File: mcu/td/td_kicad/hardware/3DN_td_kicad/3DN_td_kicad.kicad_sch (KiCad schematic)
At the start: 24 parts, among them J1 STLink, J2 ADC, J3 SPI, J4 I2C, J5 Conn_01x02, U1 STM32G031K8T6, U2 MIC5504-3.3YM5

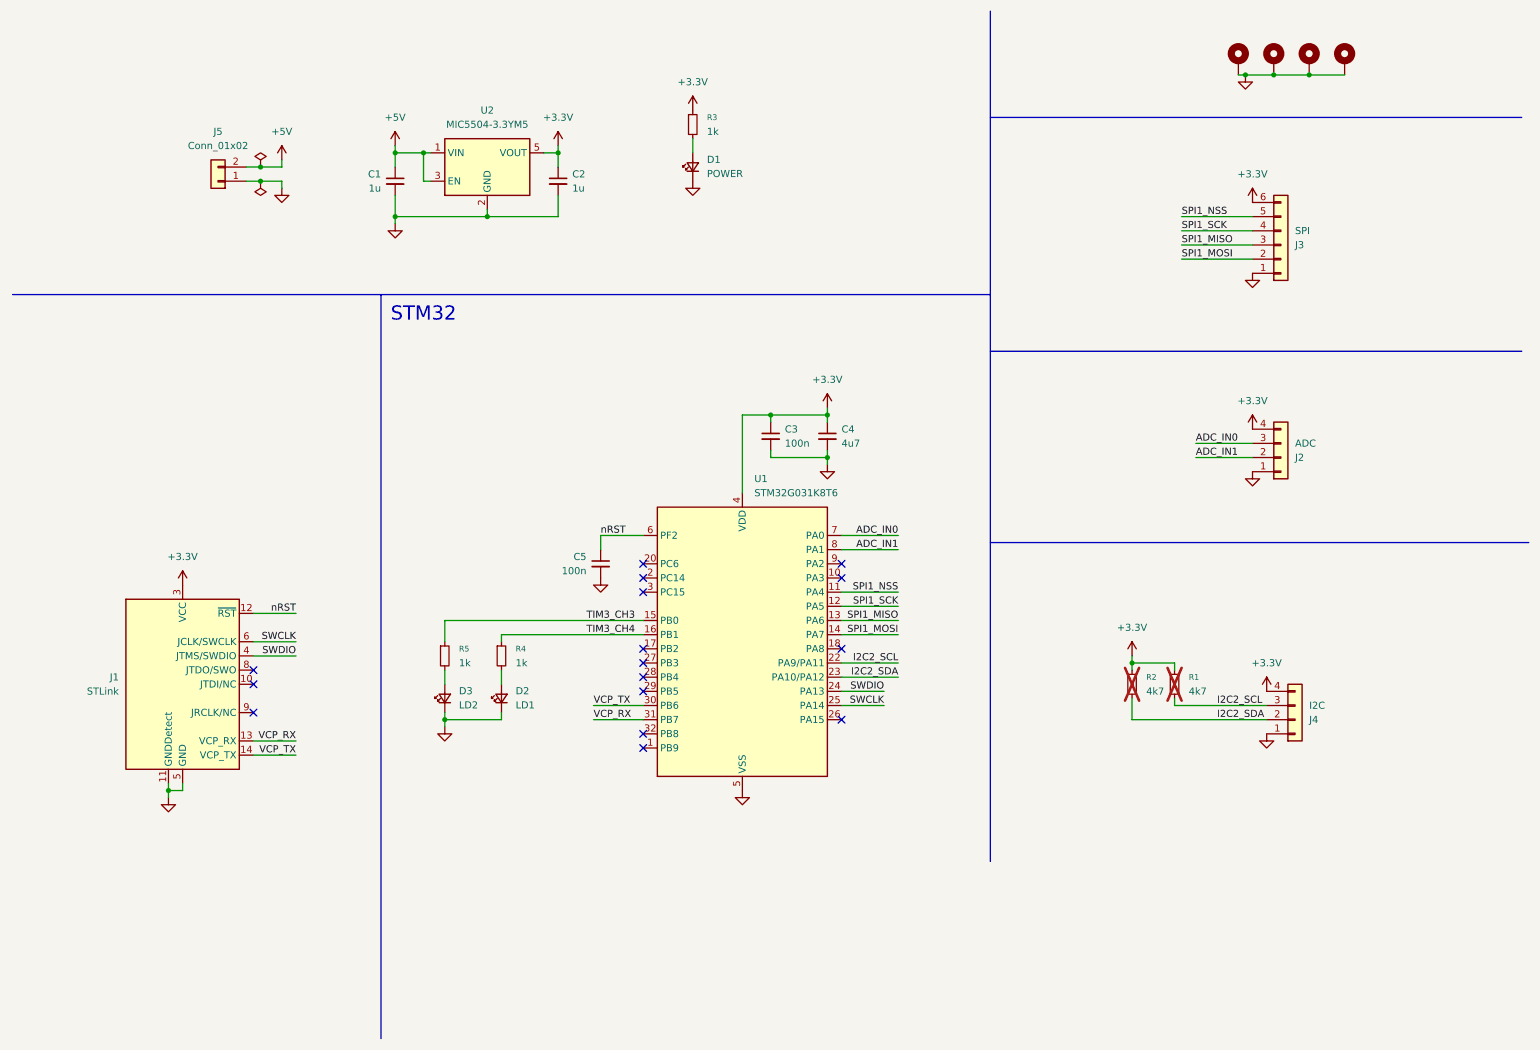
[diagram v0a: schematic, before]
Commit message: added documentation to schematic
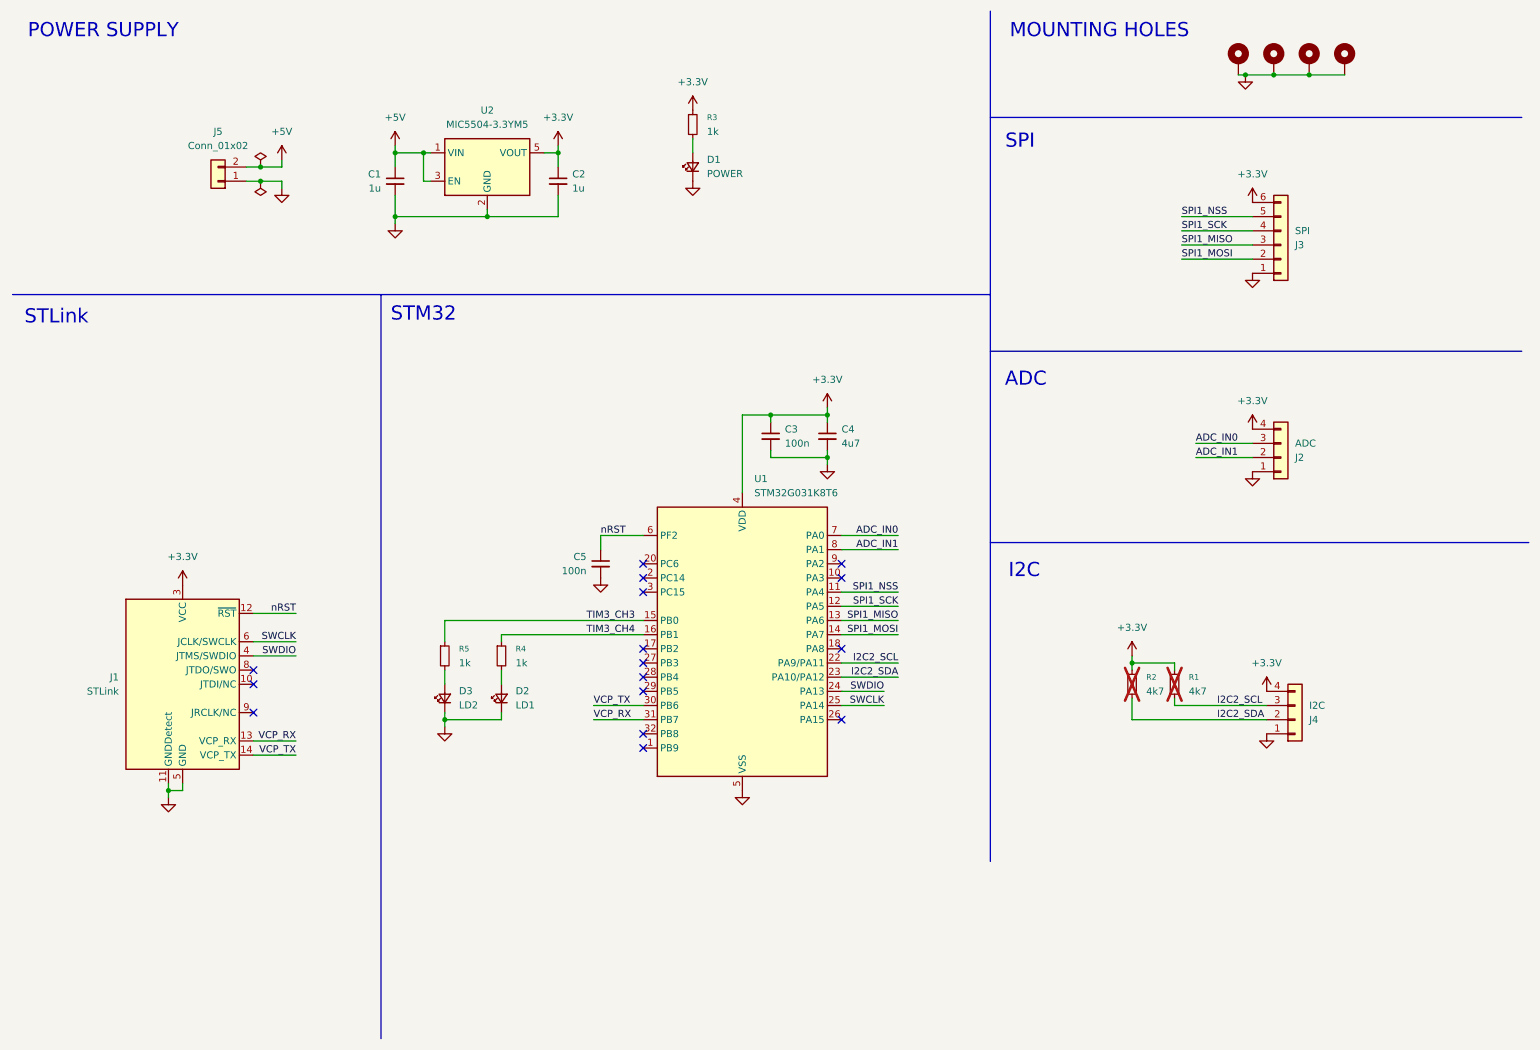
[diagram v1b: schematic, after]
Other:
- note added: "ADC"
- note added: "I2C"
- note added: "MOUNTING HOLES"
- note added: "POWER SUPPLY"
- note added: "SPI"
- note added: "STLink"
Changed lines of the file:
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@@
 		(comment 1 "Laurent Fiack")
+	)
+	(text "I2C"
+		(exclude_from_sim no)
+		(at 194.056 113.03 0)
+		(effects
+			(font
+				(size 2.54 2.54)
+			)
+		)
 	)
 	(text "STM32"
@@
 		(effects
 			(font
+				(size 2.54 2.54)
+			)
+		)
+	)
+	(text "STLink"
+		(exclude_from_sim no)
+		(at 20.574 67.564 0)
+		(effects
+			(font
+				(size 2.54 2.54)
+			)
+		)
+	)
+	(text "ADC"
+		(exclude_from_sim no)
+		(at 194.31 78.74 0)
+		(effects
+			(font
+				(size 2.54 2.54)
+			)
+		)
+	)
+	(text "SPI"
+		(exclude_from_sim no)
+		(at 193.294 36.068 0)
+		(effects
+			(font
+				(size 2.54 2.54)
+			)
+		)
+	)
+	(text "MOUNTING HOLES"
+		(exclude_from_sim no)
+		(at 207.518 16.256 0)
+		(effects
+			(font
+				(size 2.54 2.54)
+			)
+		)
+	)
+	(text "POWER SUPPLY"
+		(exclude_from_sim no)
+		(at 28.956 16.256 0)
+		(effects
+			(font
